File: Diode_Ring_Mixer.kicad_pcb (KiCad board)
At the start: 2 copper layers, 9 parts, among them J1 LO, J2 RF, J3 IF

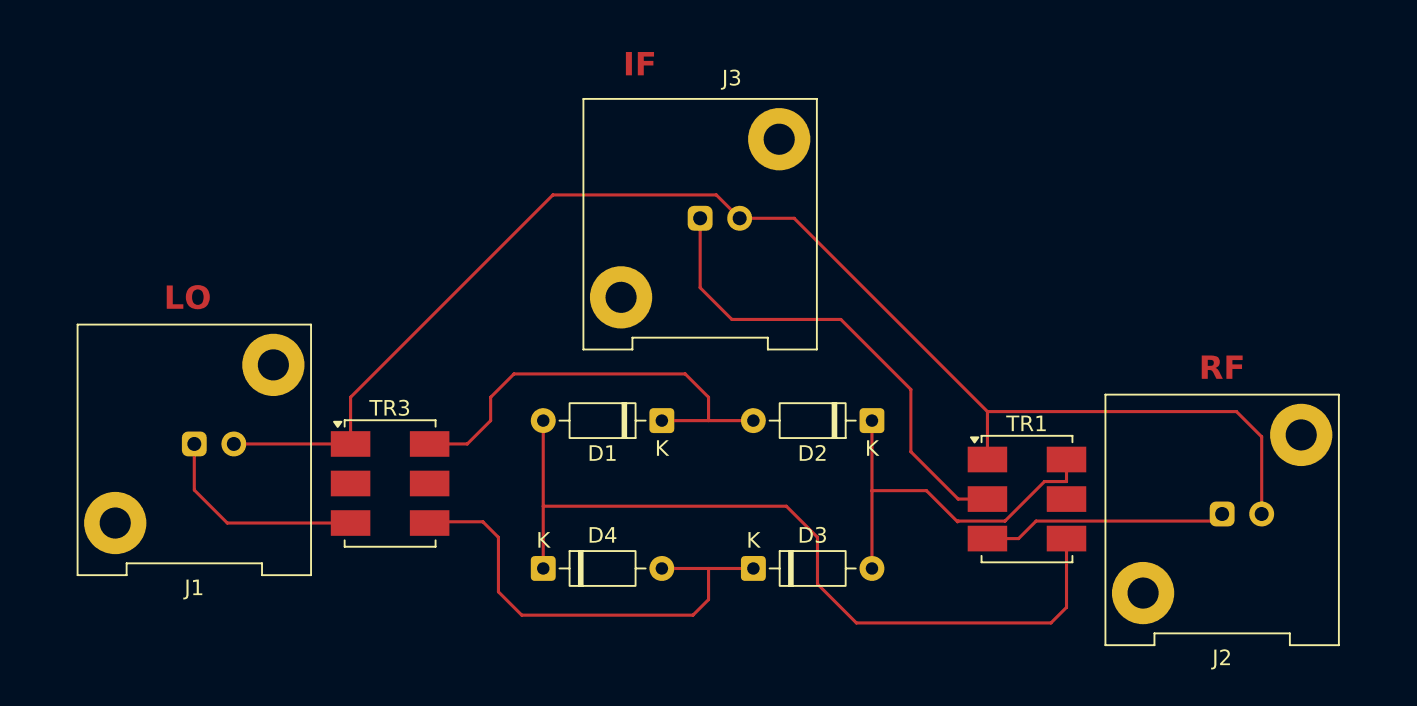
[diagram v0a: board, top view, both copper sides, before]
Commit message: Add files via upload
PCB update. added grounding plate and connection names
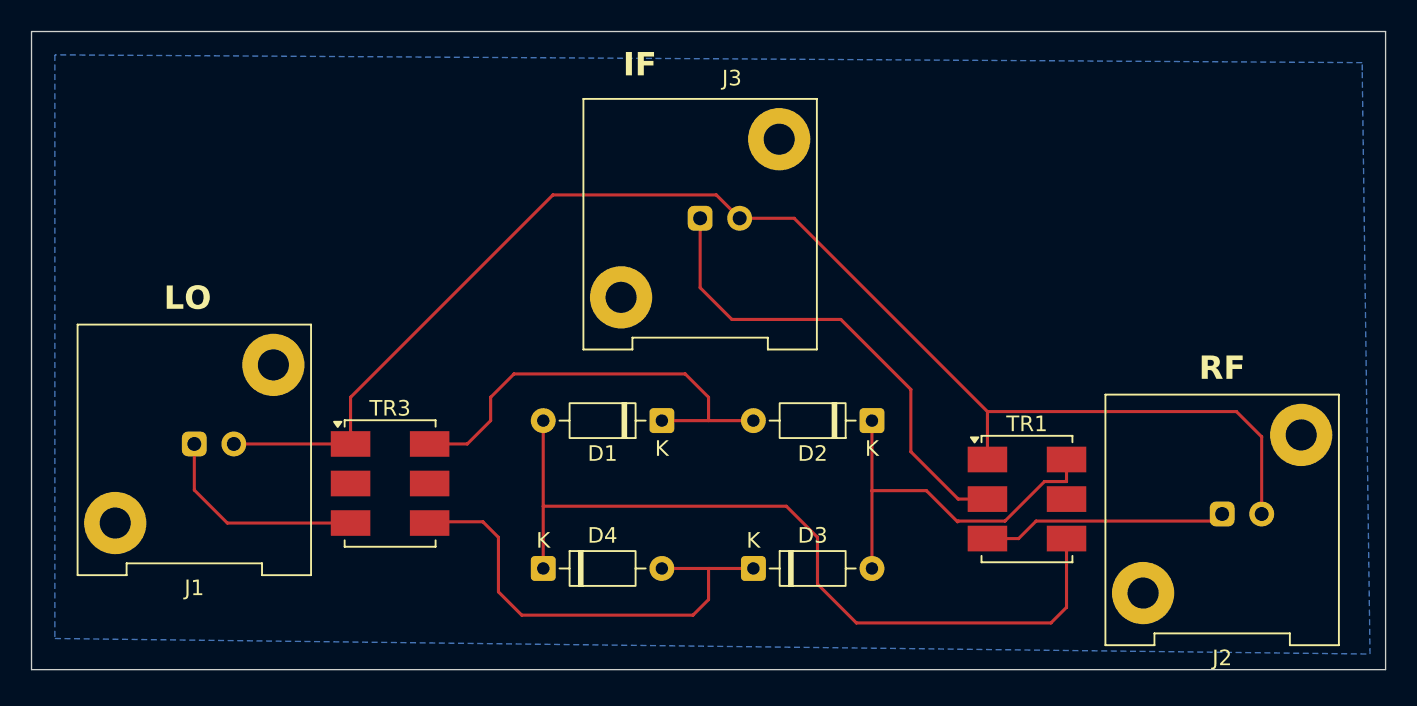
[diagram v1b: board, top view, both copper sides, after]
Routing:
- added copper zone on B.Cu, net GND
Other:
- board outline added: 87 x 41 mm
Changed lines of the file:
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@@
 		)
+	)
+	(gr_rect
+		(start 91 63.5)
+		(end 178 104.5)
+		(stroke
+			(width 0.05)
+			(type default)
+		)
+		(fill no)
+		(layer "Edge.Cuts")
 	)
 	(gr_text "LO"
 		(at 99.5 81.5 0)
-		(layer "F.Cu")
+		(layer "F.SilkS")
 		(effects
 			(font
@@
 	(gr_text "RF"
 		(at 166 86 0)
-		(layer "F.Cu")
+		(layer "F.SilkS")
 		(effects
 			(font
@@
 	(gr_text "IF"
 		(at 129 66.5 0)
-		(layer "F.Cu")
+		(layer "F.SilkS")
 		(effects
 			(font
@@
 		(net 9)
 	)
+	(zone
+		(net 6)
+		(net_name "GND")
+		(layer "B.Cu")
+		(hatch edge 0.5)
+		(connect_pads
+			(clearance 0.5)
+		)
+		(min_thickness 0.25)
+		(filled_areas_thickness no)
+		(fill yes
+			(thermal_gap 0.5)
+			(thermal_bridge_width 0.5)
+		)
+		(polygon
+			(pts
+				(xy 176.5 65.5) (xy 92.5 65) (xy 92.5 102.5) (xy 177 103.5) (xy 176.5 66)
+			)
+		)
+	)
 	(embedded_fonts no)
